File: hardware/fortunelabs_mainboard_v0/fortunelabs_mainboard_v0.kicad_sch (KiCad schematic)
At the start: 15 parts, among them J1 Conn_01x04_Pin, U1 ADS1115, U2 ESP32-S3-WROOM-2

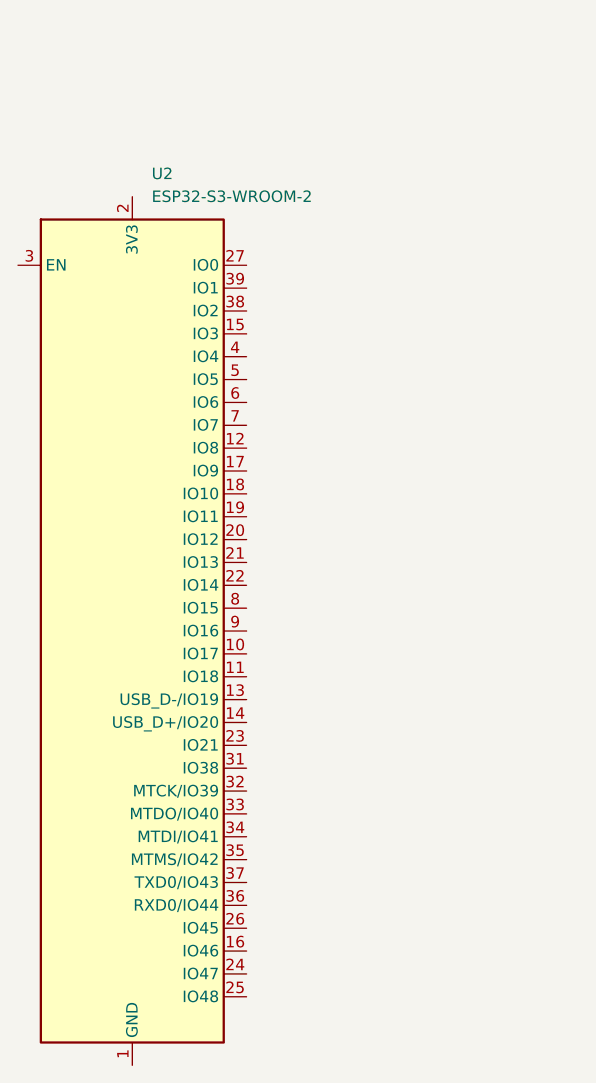
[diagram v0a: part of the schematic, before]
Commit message: feat(hardware): ads1115 schema polish
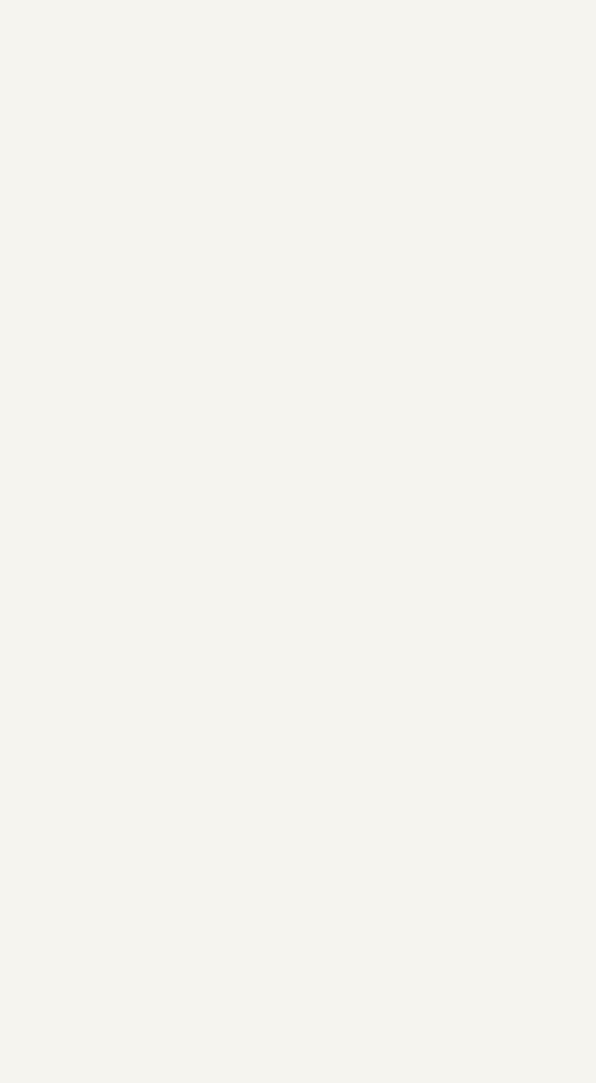
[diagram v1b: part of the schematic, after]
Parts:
- removed U2: ESP32-S3-WROOM-2, RF_Module:ESP32-S3-WROOM-2, symbol RF_Module:ESP32-S3-WROOM-2
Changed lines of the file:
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@@
-	)
-	(symbol
-		(lib_id "RF_Module:ESP32-S3-WROOM-2")
-		(at 219.71 161.29 0)
-		(unit 1)
-		(exclude_from_sim no)
-		(in_bom yes)
-		(on_board yes)
-		(dnp no)
-		(fields_autoplaced yes)
-		(property "Reference" "U2"
-			(at 221.8533 110.49 0)
-			(effects
-				(font
-					(size 1.27 1.27)
-				)
-				(justify left)
-			)
-		)
-		(property "Value" "ESP32-S3-WROOM-2"
-			(at 221.8533 113.03 0)
-			(effects
-				(font
-					(size 1.27 1.27)
-				)
-				(justify left)
-			)
-		)
-		(property "Footprint" "RF_Module:ESP32-S3-WROOM-2"
-			(at 219.71 222.25 0)
-			(effects
-				(font
-					(size 1.27 1.27)
-				)
-				(hide yes)
-			)
-		)
-		(property "Datasheet" "https://www.espressif.com/sites/default/files/documentation/esp32-s3-wroom-2_datasheet_en.pdf"
-			(at 219.71 224.79 0)
-			(effects
-				(font
-					(size 1.27 1.27)
-				)
-				(hide yes)
-			)
-		)
-		(property "Description" "RF Module, 2.4 GHz, Wi­-Fi, Bluetooth, BLE, ESP32­-S3R8V"
-			(at 219.71 161.29 0)
-			(effects
-				(font
-					(size 1.27 1.27)
-				)
-				(hide yes)
-			)
-		)
-		(pin "23"
-		)
-		(pin "27"
-		)
-		(pin "20"
-		)
-		(pin "40"
-		)
-		(pin "30"
-		)
-		(pin "8"
-		)
-		(pin "7"
-		)
-		(pin "39"
-		)
-		(pin "9"
-		)
-		(pin "34"
-		)
-		(pin "14"
-		)
-		(pin "35"
-		)
-		(pin "25"
-		)
-		(pin "17"
-		)
-		(pin "5"
-		)
-		(pin "13"
-		)
-		(pin "12"
-		)
-		(pin "32"
-		)
-		(pin "11"
-		)
-		(pin "10"
-		)
-		(pin "3"
-		)
-		(pin "31"
-		)
-		(pin "33"
-		)
-		(pin "38"
-		)
-		(pin "26"
-		)
-		(pin "16"
-		)
-		(pin "15"
-		)
-		(pin "41"
-		)
-		(pin "37"
-		)
-		(pin "6"
-		)
-		(pin "28"
-		)
-		(pin "29"
-		)
-		(pin "2"
-		)
-		(pin "1"
-		)
-		(pin "21"
-		)
-		(pin "19"
-		)
-		(pin "22"
-		)
-		(pin "18"
-		)
-		(pin "24"
-		)
-		(pin "36"
-		)
-		(pin "4"
-		)
-		(instances
-			(project "fortunelabs_mainboard_v0"
-				(path "/1727eecb-65c8-4b57-aa8a-814f366e0831"
-					(reference "U2")
-					(unit 1)
-				)
-			)
-		)
 	)
 	(symbol

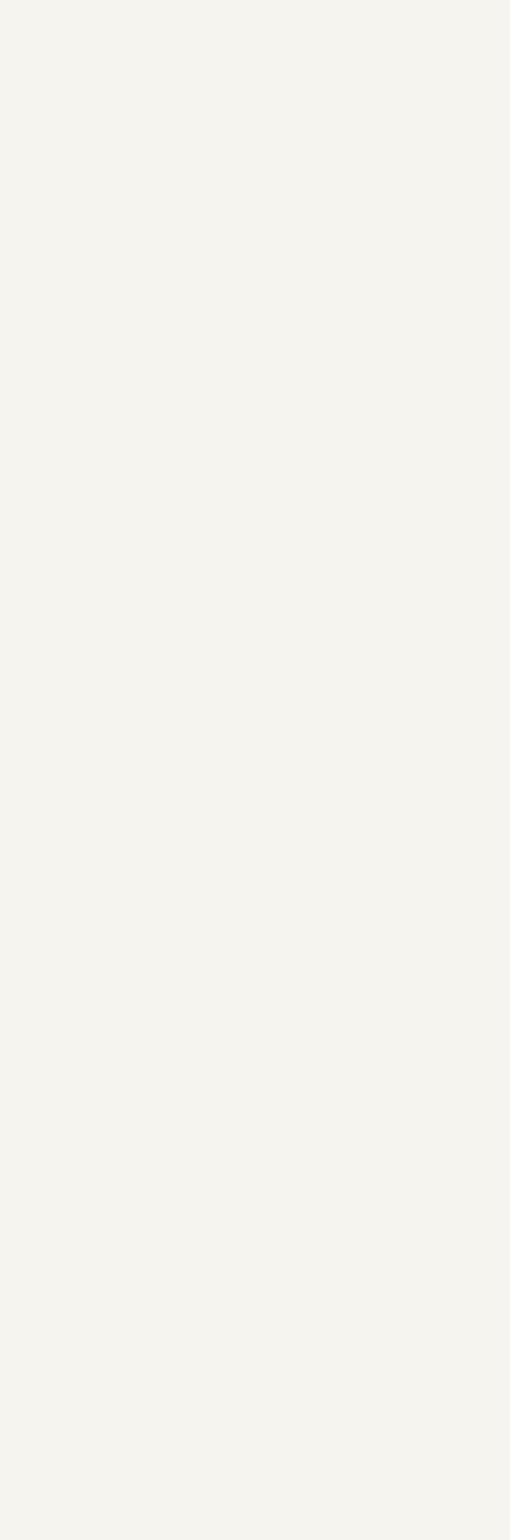
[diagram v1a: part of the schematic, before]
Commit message: feat: add ic block scaffold
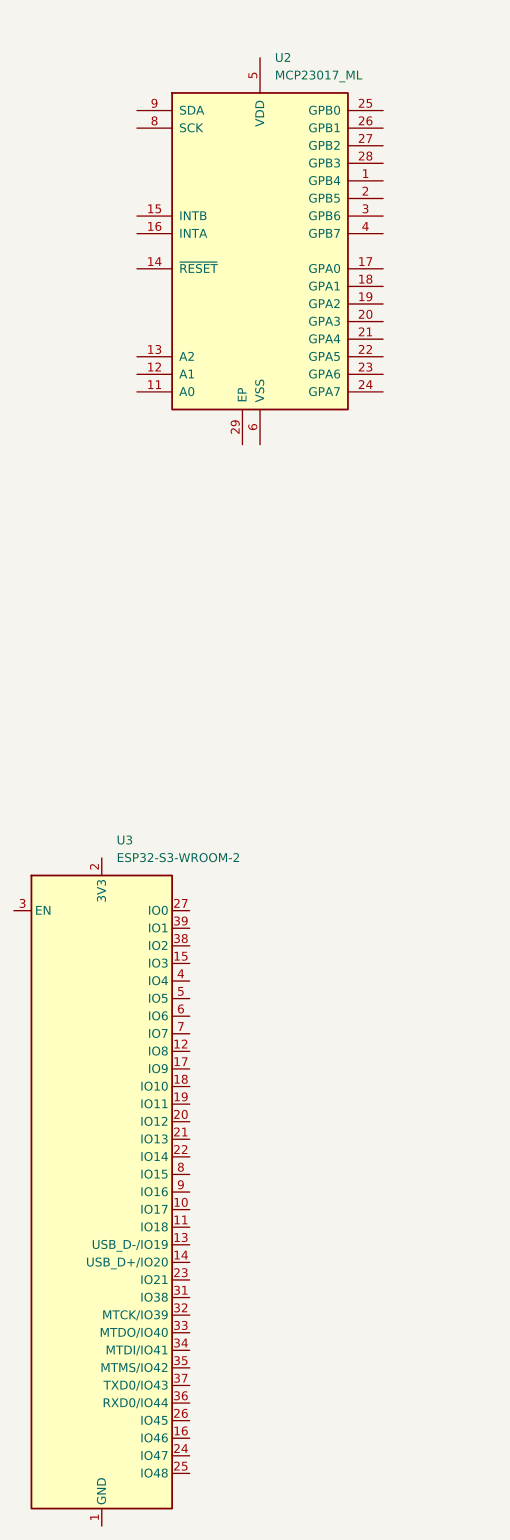
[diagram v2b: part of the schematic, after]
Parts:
- added U2: MCP23017_ML, Package_DFN_QFN:QFN-28-1EP_6x6mm_P0.65mm_EP4.25x4.25mm, symbol Interface_Expansion:MCP23017_ML
- added U3: ESP32-S3-WROOM-2, RF_Module:ESP32-S3-WROOM-2, symbol RF_Module:ESP32-S3-WROOM-2
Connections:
- new net: U3.1 (GND), U3.40 (GND), U3.41 (GND)

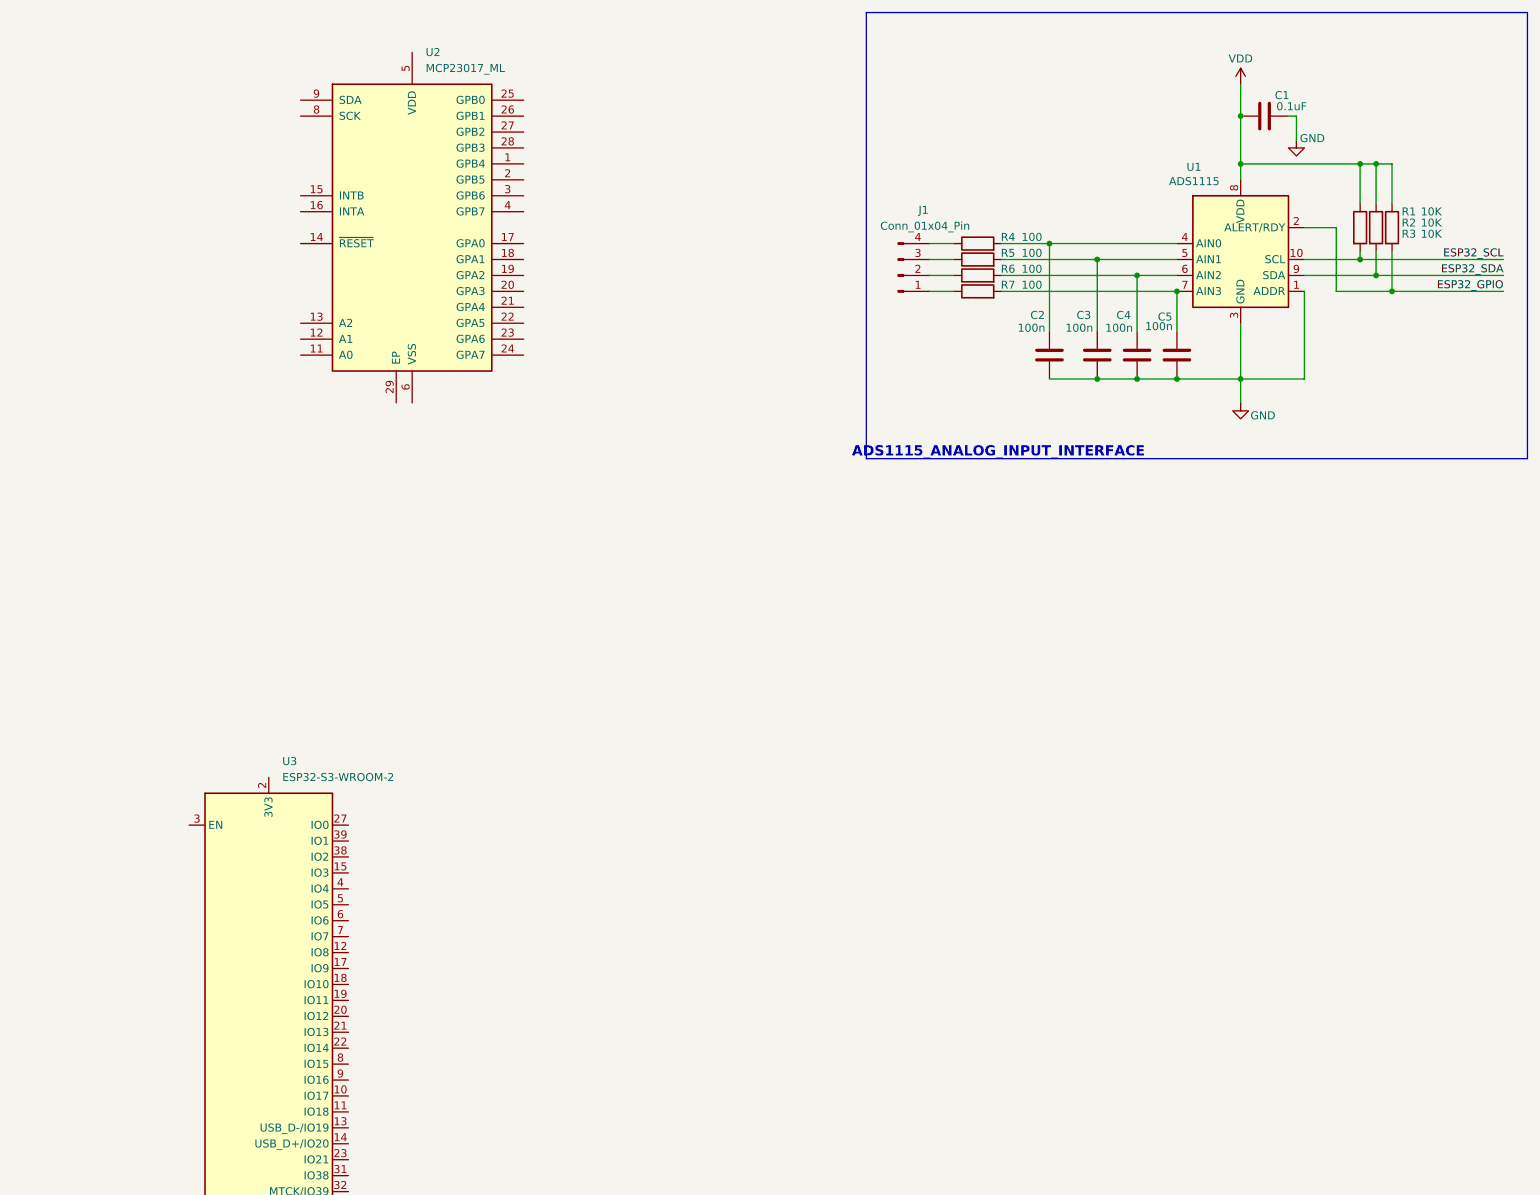
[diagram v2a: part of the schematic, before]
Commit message: feat: designing mcp23017 init schematic
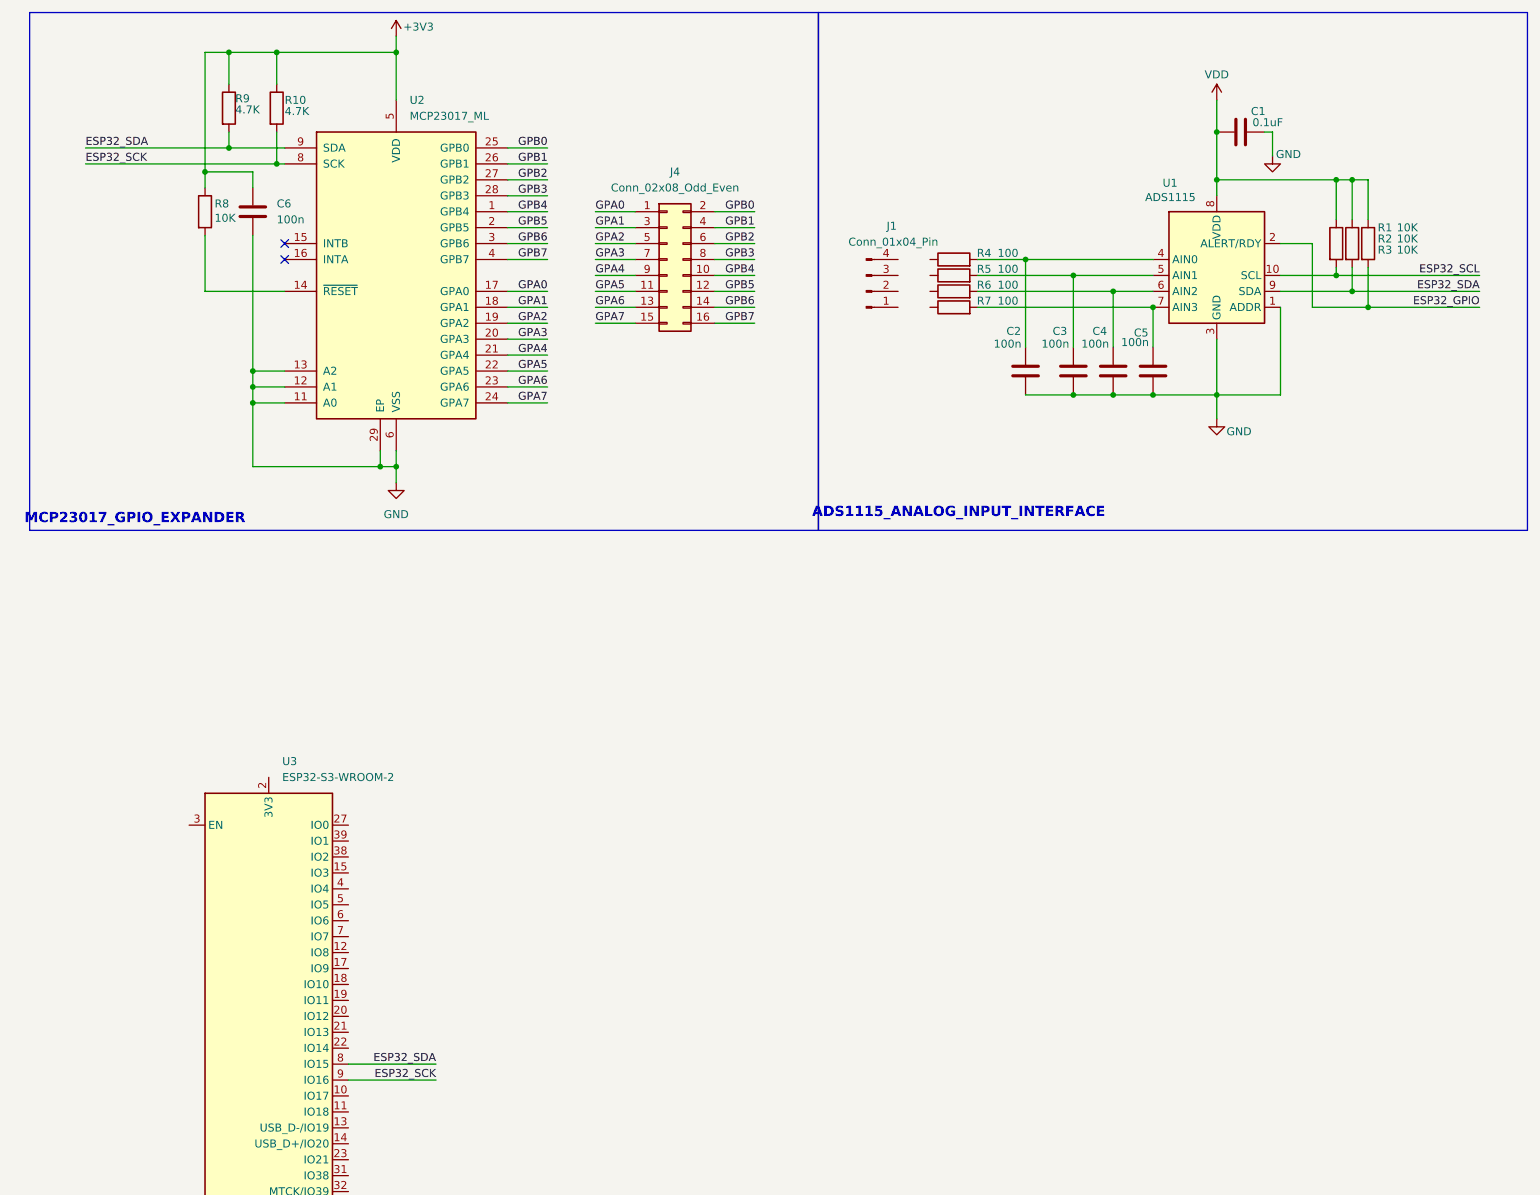
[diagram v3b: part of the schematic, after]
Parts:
- added C6: 100n, symbol Device:C
- added J4: Conn_02x08_Odd_Even, symbol Connector_Generic:Conn_02x08_Odd_Even
- added R10, R9: 4.7K, symbol Device:R
- added R8: 10K, symbol Device:R
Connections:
- net ESP32_SDA: now also U2.9 (SDA), U3.8 (IO15), R9.2
- net GND: now also U2.11 (A0), U2.12 (A1), U2.13 (A2), U2.29 (EP), U2.6 (VSS), C6.2
- net ESP32_SCK: now reaches U3.9 (IO16)
- net ESP32_SCK: now also U2.8 (SCK), R10.2
- net at R6.1: no longer J1.2 (Pin_2)
- net at R4.1: no longer J1.4 (Pin_4)
- net at R5.1: no longer J1.3 (Pin_3)
- net GPB4: now reaches U2.1 (GPB4)
- net GPB4: now also J4.10 (Pin_10)
- net at U2.14 (~{RESET}): now also R8.2
- net GPA0: now reaches U2.17 (GPA0)
- net GPA0: now also J4.1 (Pin_1)
- net GPA1: now reaches U2.18 (GPA1)
- net GPA1: now also J4.3 (Pin_3)
- net GPA2: now reaches U2.19 (GPA2)
- net GPA2: now also J4.5 (Pin_5)
- net GPB5: now reaches U2.2 (GPB5)
- net GPB5: now also J4.12 (Pin_12)
- net GPA3: now reaches U2.20 (GPA3)
- net GPA3: now also J4.7 (Pin_7)
- net GPA4: now reaches U2.21 (GPA4)
- net GPA4: now also J4.9 (Pin_9)
- net GPA5: now reaches U2.22 (GPA5)
- net GPA5: now also J4.11 (Pin_11)
- net GPA6: now reaches U2.23 (GPA6)
- net GPA6: now also J4.13 (Pin_13)
- net GPA7: now reaches U2.24 (GPA7)
- net GPA7: now also J4.15 (Pin_15)
- net GPB0: now reaches U2.25 (GPB0)
- net GPB0: now also J4.2 (Pin_2)
- net GPB1: now reaches U2.26 (GPB1)
- net GPB1: now also J4.4 (Pin_4)
- net GPB2: now reaches U2.27 (GPB2)
- net GPB2: now also J4.6 (Pin_6)
- net GPB3: now reaches U2.28 (GPB3)
- net GPB3: now also J4.8 (Pin_8)
- net GPB6: now reaches U2.3 (GPB6)
- net GPB6: now also J4.14 (Pin_14)
- net GPB7: now reaches U2.4 (GPB7)
- net GPB7: now also J4.16 (Pin_16)
- net +3V3: now reaches U2.5 (VDD)
- net +3V3: now also C6.1, R10.1, R8.1, R9.1
- net at J1.1 (Pin_1): no longer R7.1
- no-connect marks 0 -> 2
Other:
- note added: "MCP23017_GPIO_EXPANDER"
- moved on the sheet: C1, C2, C3, C4, C5, J1, R1, R2, R3, R4, R5, R6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
